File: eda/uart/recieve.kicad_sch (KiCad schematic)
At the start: 0 parts

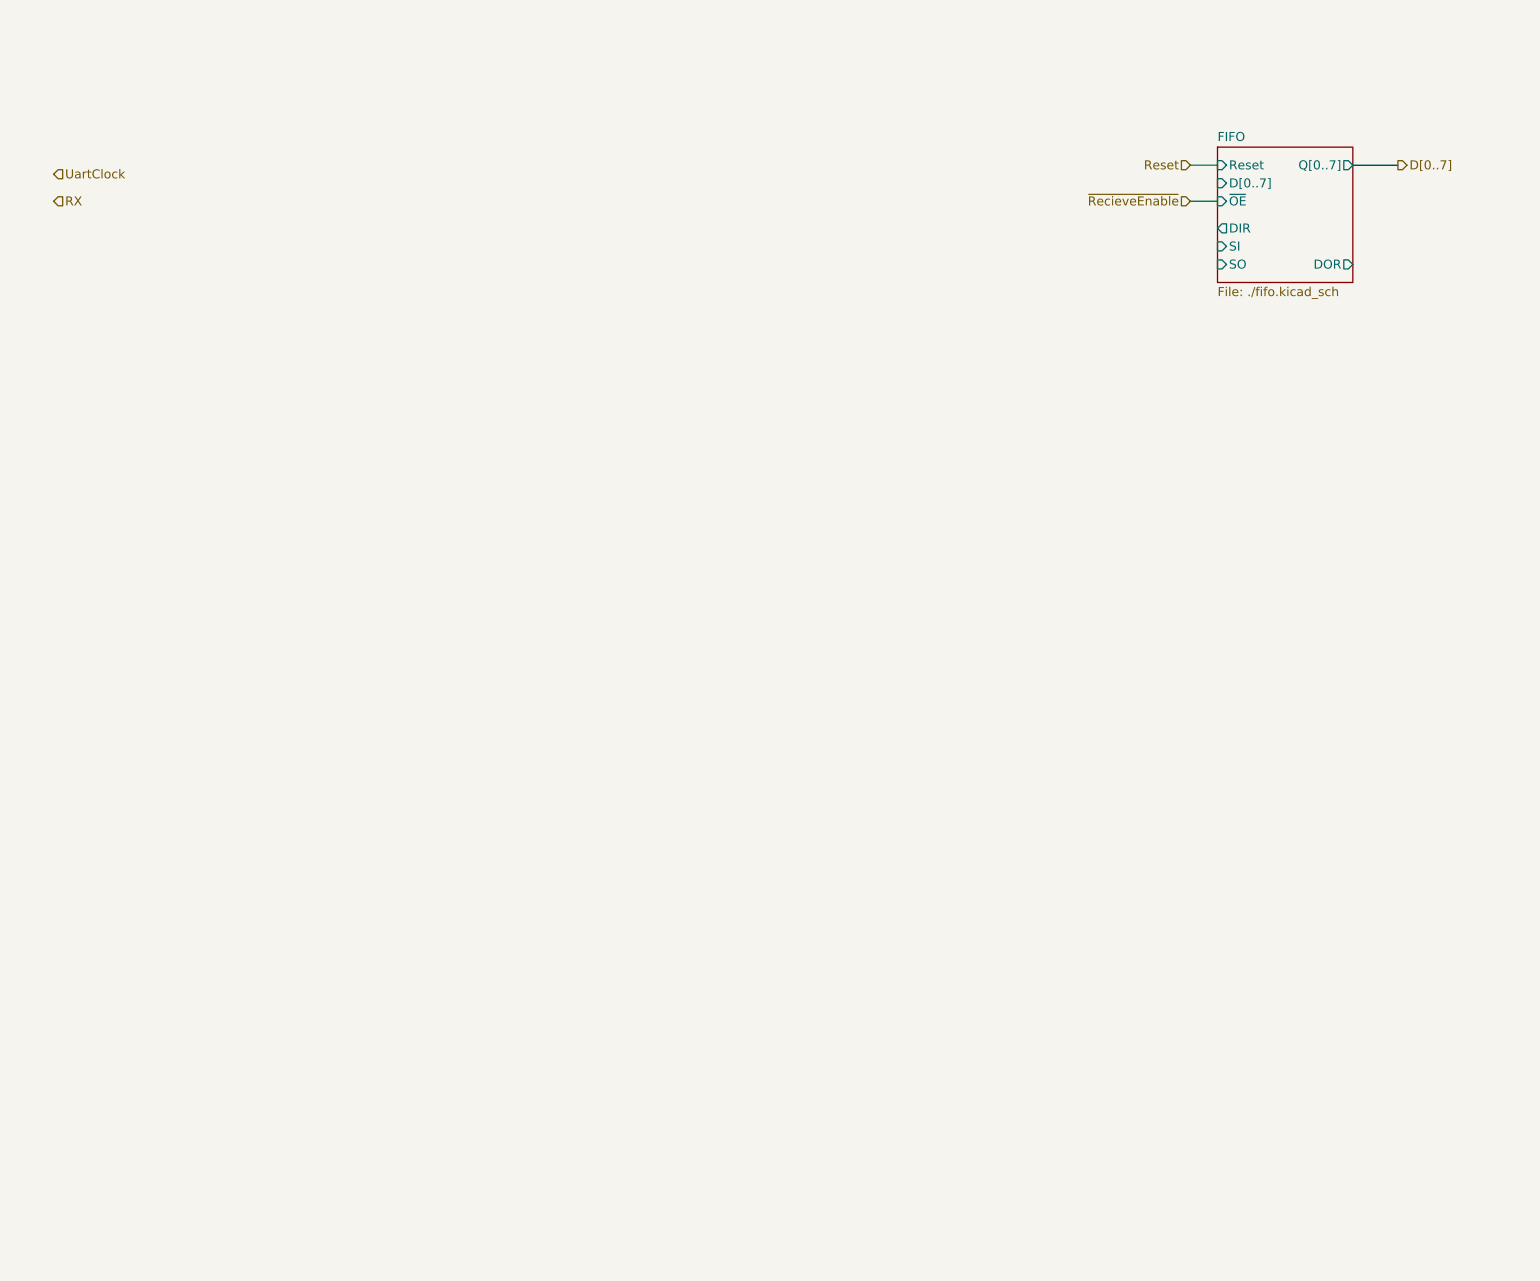
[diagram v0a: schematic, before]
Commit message: Port main board schematic to kicad
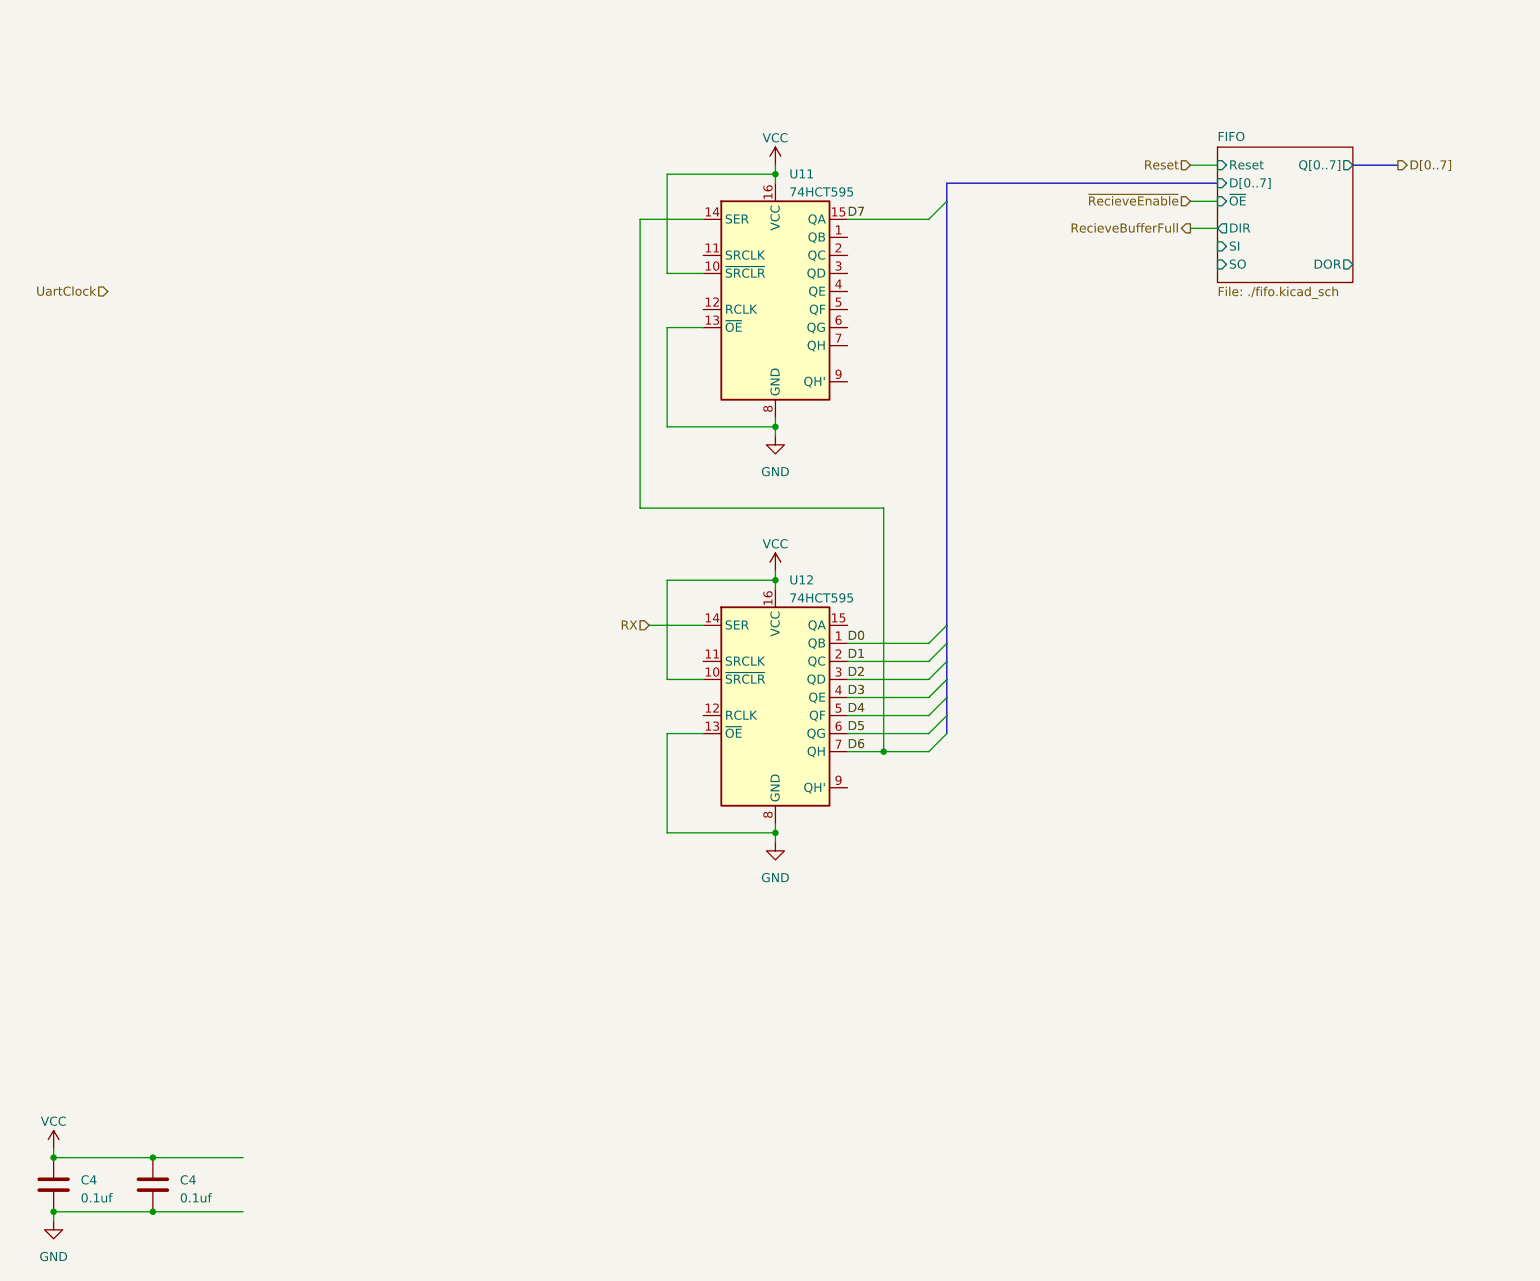
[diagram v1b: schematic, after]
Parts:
- added C4 (x2): 0.1uf, Capacitor_THT:C_Rect_L7.2mm_W3.5mm_P5.00mm_FKS2_FKP2_MKS2_MKP2, symbol Device:C
- added U11, U12: 74HCT595, Package_DIP:DIP-16_W7.62mm, symbol 74xx:74LS595
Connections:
- net RX: now also U12.14 (SER)
- new net D0: U12.1 (QB)
- new net D1: U12.2 (QC)
- new net D2: U12.3 (QD)
- new net D3: U12.4 (QE)
- new net D4: U12.5 (QF)
- new net D5: U12.6 (QG)
- new net D6: U11.14 (SER), U12.7 (QH)
- new net D7: U11.15 (QA)
- new net GND: C4.2, C4.2, U11.13 (~{OE}), U11.8 (GND), U12.13 (~{OE}), U12.8 (GND)
- new net VCC: C4.1, C4.1, U11.10 (~{SRCLR}), U11.16 (VCC), U12.10 (~{SRCLR}), U12.16 (VCC)

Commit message: Work on main board eda, interim
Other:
- sheet FIFO renamed FIFO Recieve
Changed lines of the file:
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@@
     (stroke (width 0) (type default))
   )
-  (label "D2" (at 144.78 106.68 0)
-    (effects (font (size 1.27 1.27)) (justify left bottom))
-  )
-  (label "D7" (at 144.78 41.91 0)
-    (effects (font (size 1.27 1.27)) (justify left bottom))
-  )
-  (label "D5" (at 144.78 114.3 0)
-    (effects (font (size 1.27 1.27)) (justify left bottom))
-  )
-  (label "D1" (at 144.78 104.14 0)
-    (effects (font (size 1.27 1.27)) (justify left bottom))
-  )
-  (label "D4" (at 144.78 111.76 0)
-    (effects (font (size 1.27 1.27)) (justify left bottom))
-  )
-  (label "D3" (at 144.78 109.22 0)
-    (effects (font (size 1.27 1.27)) (justify left bottom))
-  )
-  (label "D6" (at 144.78 116.84 0)
-    (effects (font (size 1.27 1.27)) (justify left bottom))
-  )
-  (label "D0" (at 144.78 101.6 0)
+  (label "D2" (at 144.78 106.68 0) (fields_autoplaced)
+    (effects (font (size 1.27 1.27)) (justify left bottom))
+  )
+  (label "D7" (at 144.78 41.91 0) (fields_autoplaced)
+    (effects (font (size 1.27 1.27)) (justify left bottom))
+  )
+  (label "D5" (at 144.78 114.3 0) (fields_autoplaced)
+    (effects (font (size 1.27 1.27)) (justify left bottom))
+  )
+  (label "D1" (at 144.78 104.14 0) (fields_autoplaced)
+    (effects (font (size 1.27 1.27)) (justify left bottom))
+  )
+  (label "D4" (at 144.78 111.76 0) (fields_autoplaced)
+    (effects (font (size 1.27 1.27)) (justify left bottom))
+  )
+  (label "D3" (at 144.78 109.22 0) (fields_autoplaced)
+    (effects (font (size 1.27 1.27)) (justify left bottom))
+  )
+  (label "D6" (at 146.05 116.84 0) (fields_autoplaced)
+    (effects (font (size 1.27 1.27)) (justify left bottom))
+  )
+  (label "D0" (at 144.78 101.6 0) (fields_autoplaced)
     (effects (font (size 1.27 1.27)) (justify left bottom))
   )
@@
     (effects (font (size 1.27 1.27)) (justify right))
   )
-  (hierarchical_label "D[0..7]" (shape output) (at 222.25 34.29 0) (fields_autoplaced)
+  (hierarchical_label "DOut[0..7]" (shape output) (at 222.25 34.29 0) (fields_autoplaced)
     (effects (font (size 1.27 1.27)) (justify left))
   )
@@
     (stroke (width 0.1524) (type solid))
     (fill (color 0 0 0 0.0000))
-    (property "Sheetname" "FIFO" (at 196.85 31.0384 0)
+    (property "Sheetname" "FIFO Recieve" (at 196.85 31.0384 0)
       (effects (font (size 1.27 1.27)) (justify left bottom))
     )

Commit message: Update eda
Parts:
- added U1: 74HCT193, Package_DIP:DIP-16_W7.62mm, symbol 74xx:74LS193
- added U15 (x2): 74HCT00, symbol 74xx:74HCT00
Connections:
- net GND: now also U1.1 (B), U1.10 (C), U1.14 (CLR), U1.15 (A), U1.5 (UP), U1.8 (GND)
- net RX: now also U15.1
- net Reset: now also U1.13 (~{BO}), U15.2
- net UartClock: now also U11.11 (SRCLK), U11.12 (RCLK), U12.11 (SRCLK), U12.12 (RCLK), U1.4 (DOWN)
- net VCC: now also U1.16 (VCC), U1.9 (D); no longer U11.10 (~{SRCLR}), U12.10 (~{SRCLR})
- new net: U11.10 (~{SRCLR}), U12.10 (~{SRCLR}), U15.2, U15.3
- new net: U1.11 (~{LOAD}), U15.1, U15.3
- no-connect marks 0 -> 13

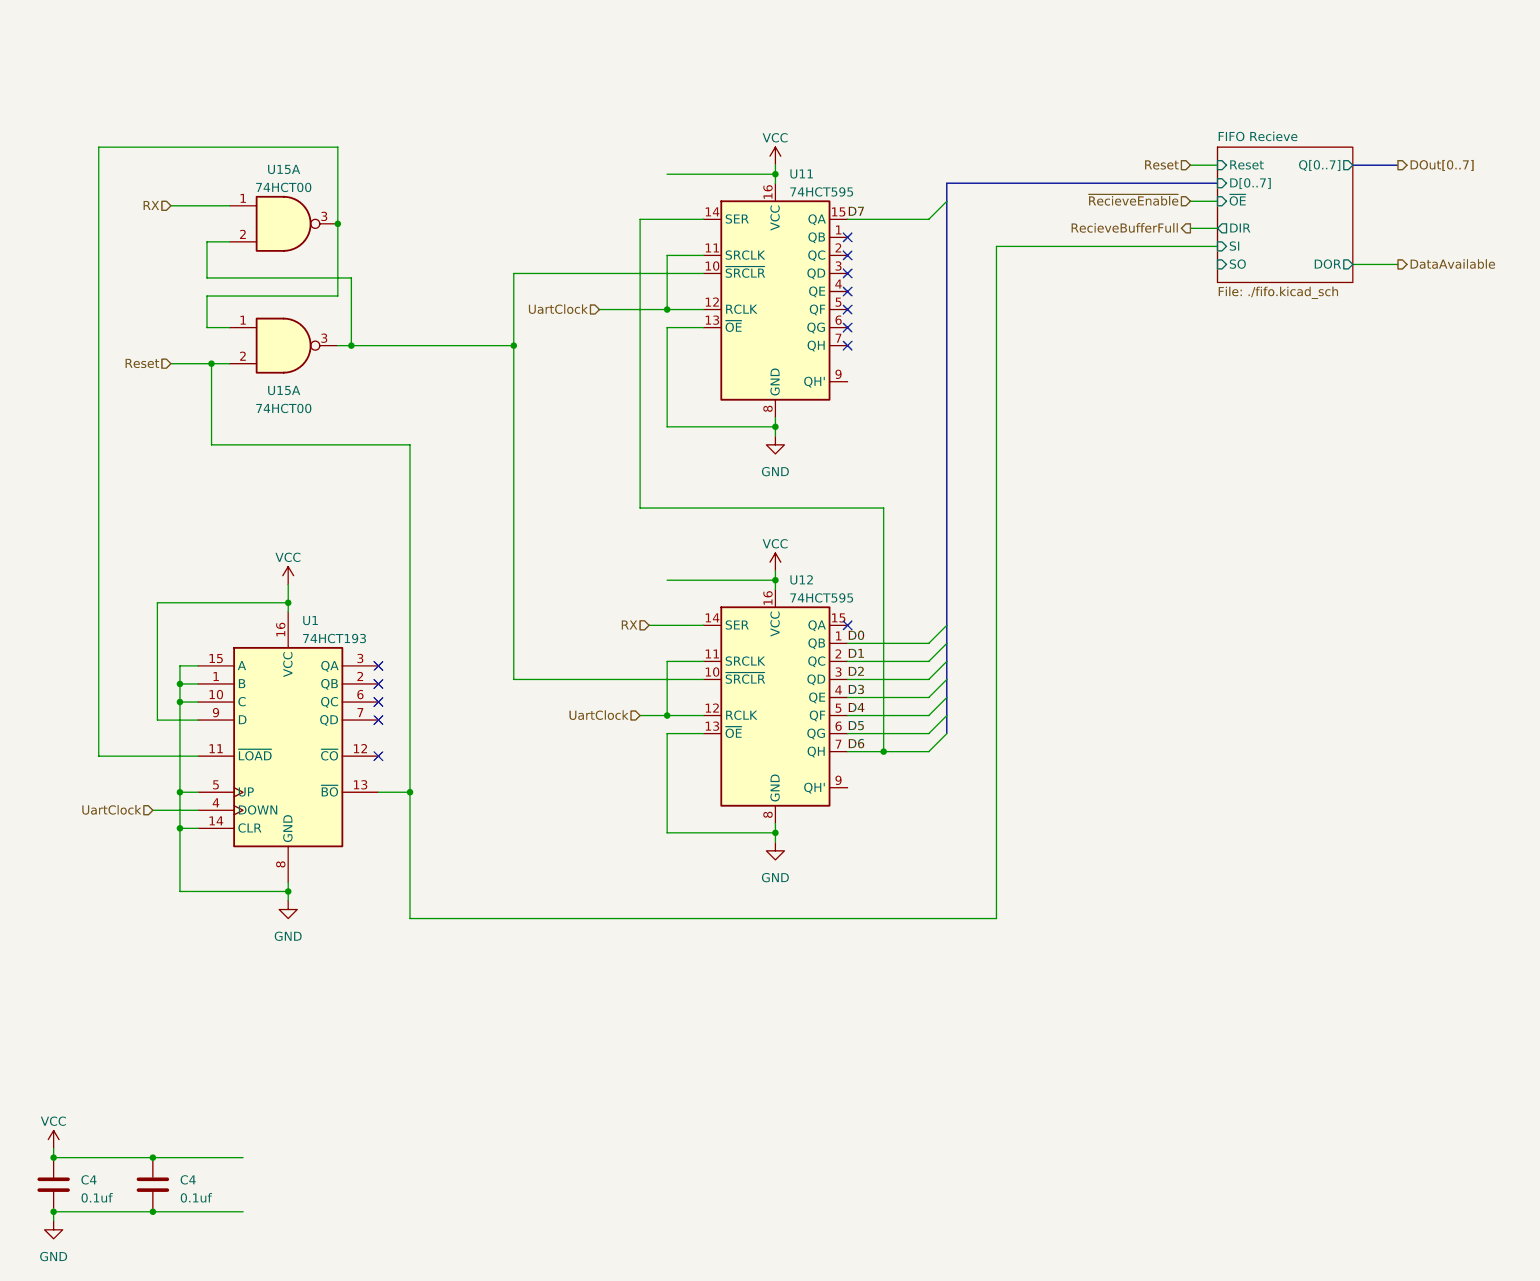
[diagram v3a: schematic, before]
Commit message: Convert expansion breakout to kicad
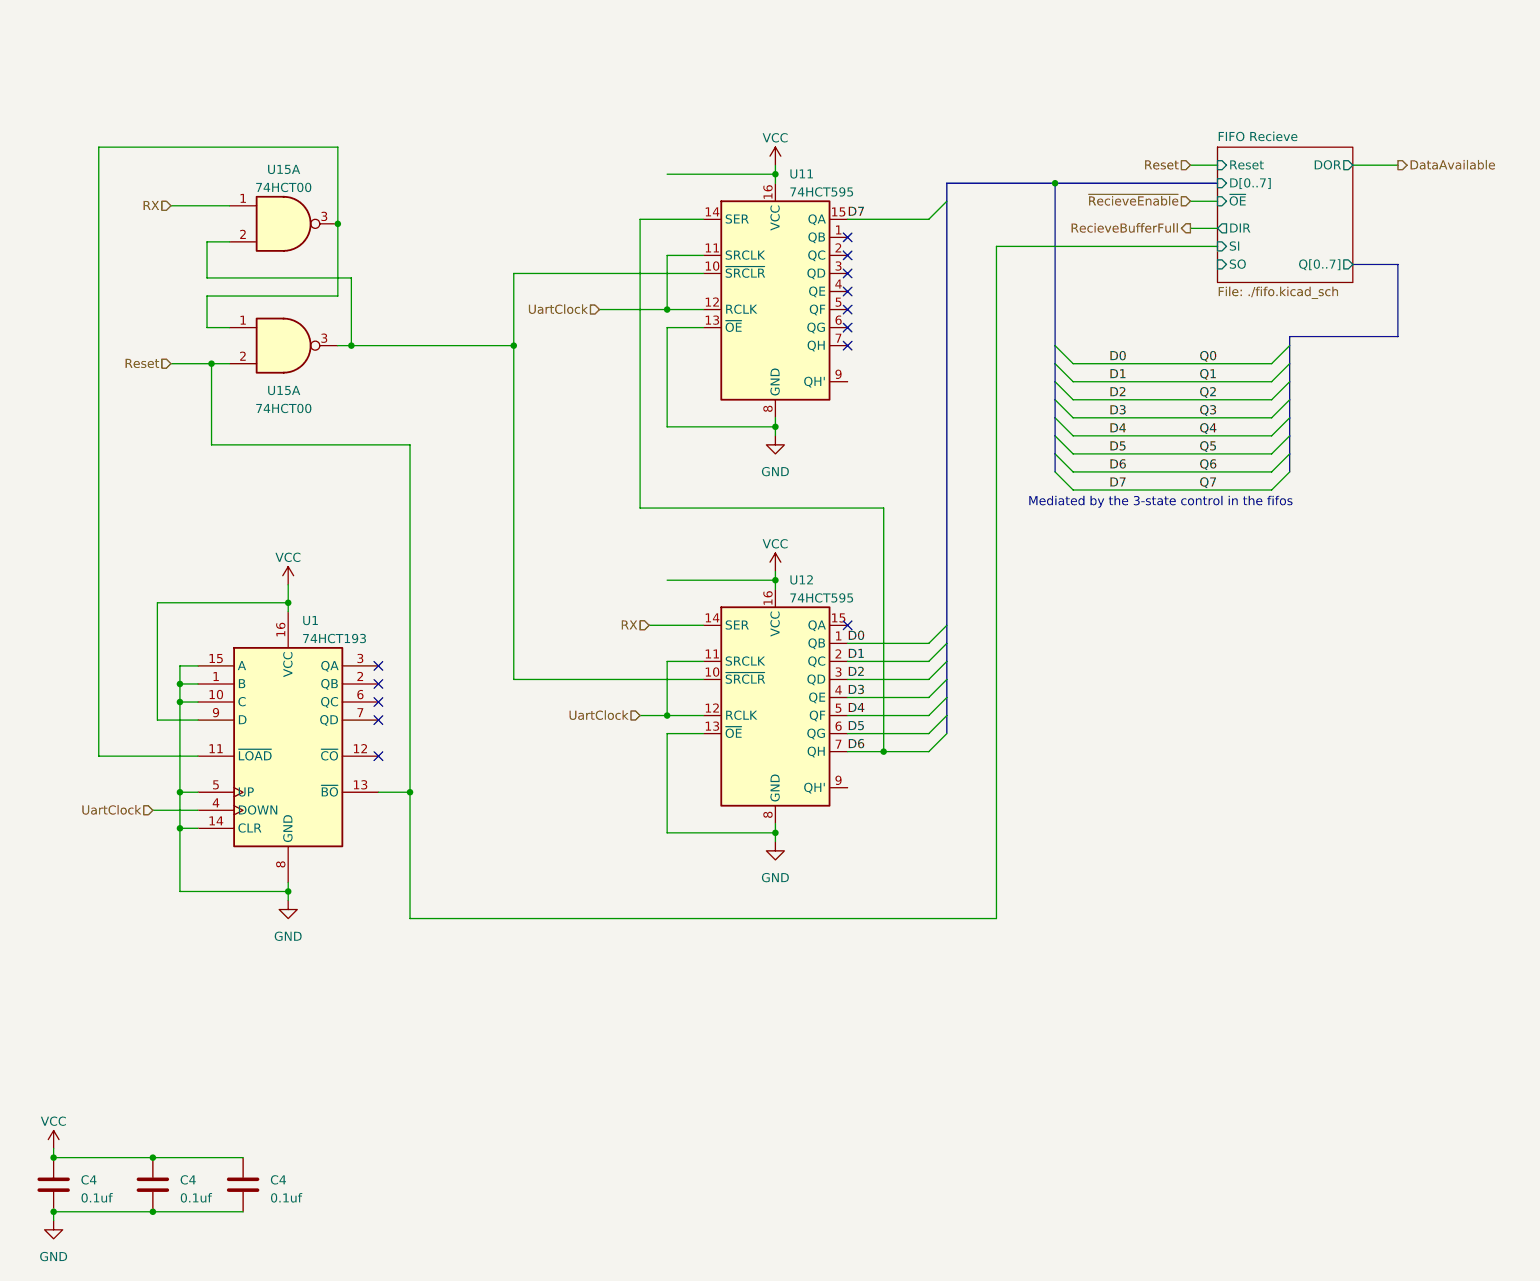
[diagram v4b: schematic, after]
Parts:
- added C4: 0.1uf, Capacitor_THT:C_Rect_L7.2mm_W3.5mm_P5.00mm_FKS2_FKP2_MKS2_MKP2, symbol Device:C
- U15: footprint (none) -> Package_DIP:DIP-14_W7.62mm
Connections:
- net GND: now also C4.2
- net VCC: now also C4.1
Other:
- note added: "Mediated by the 3-state control in the fifos"

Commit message: Sync
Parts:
- added D1: 1N4001, Diode_THT:D_DO-41_SOD81_P10.16mm_Horizontal, symbol Diode:1N4001
- added R1: 10K, Resistor_THT:R_Axial_DIN0207_L6.3mm_D2.5mm_P7.62mm_Horizontal, symbol Device:R
- added U2: 74HCT14, Package_DIP:DIP-14_W7.62mm, symbol 74xx:74LS14
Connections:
- net Reset: no longer U1.13 (~{BO}), U15.2
- net VCC: now also R1.1
- net at U11.10 (~{SRCLR}), U12.10 (~{SRCLR}): now also U1.11 (~{LOAD}), U15.1, U15.3; no longer U15.2, U15.3
- new net: D1.2 (A), R1.2, U1.13 (~{BO}), U15.2, U2.3
- new net: U15.2, U15.3
- new net FIFO Recieve/SI: U2.4
- new net ~{Reset}: D1.1 (K)
- no-connect marks 13 -> 15

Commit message: Branch of uart to v1
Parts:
- removed D1: 1N4001, Diode_THT:D_DO-41_SOD81_P10.16mm_Horizontal, symbol Diode:1N4001
- removed R1: 10K, Resistor_THT:R_Axial_DIN0207_L6.3mm_D2.5mm_P7.62mm_Horizontal, symbol Device:R
- added unit 6 of U2
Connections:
- net D6: no longer U11.14 (SER)
- net GND: no longer U1.5 (UP)
- net VCC: now also U1.5 (UP)
- net ~{RecieveEnable}: now also U2.13
- net at U12.9 (QH'): now also U11.14 (SER)
- no-connect marks 15 -> 14

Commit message: Normalize cap size
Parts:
- C4: footprint Capacitor_THT:C_Rect_L7.2mm_W3.5mm_P5.00mm_FKS2_FKP2_MKS2_MKP2 -> Capacitor_THT:C_Disc_D3.8mm_W2.6mm_P2.50mm
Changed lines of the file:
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@@
       (effects (font (size 1.27 1.27)) (justify left))
     )
-    (property "Footprint" "Capacitor_THT:C_Rect_L7.2mm_W3.5mm_P5.00mm_FKS2_FKP2_MKS2_MKP2" (at 60.6552 181.61 0)
+    (property "Footprint" "Capacitor_THT:C_Disc_D3.8mm_W2.6mm_P2.50mm" (at 60.6552 181.61 0)
       (effects (font (size 1.27 1.27)) hide)
     )
@@
       (effects (font (size 1.27 1.27)) (justify left))
     )
-    (property "Footprint" "Capacitor_THT:C_Rect_L7.2mm_W3.5mm_P5.00mm_FKS2_FKP2_MKS2_MKP2" (at 47.9552 181.61 0)
+    (property "Footprint" "Capacitor_THT:C_Disc_D3.8mm_W2.6mm_P2.50mm" (at 47.9552 181.61 0)
       (effects (font (size 1.27 1.27)) hide)
     )
@@
       (effects (font (size 1.27 1.27)) (justify left))
     )
-    (property "Footprint" "Capacitor_THT:C_Rect_L7.2mm_W3.5mm_P5.00mm_FKS2_FKP2_MKS2_MKP2" (at 33.9852 181.61 0)
-      (effects (font (size 1.27 1.27)) hide)
-    )
+    (property "Footprint" "Capacitor_THT:C_Disc_D3.8mm_W2.6mm_P2.50mm" (at 33.9852 181.61 0)
+      (effects (font (size 1.27 1.27)) hide)
+    )
